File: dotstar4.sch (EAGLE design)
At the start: 13 parts, among them J1 IN/OUT, J2 OUT

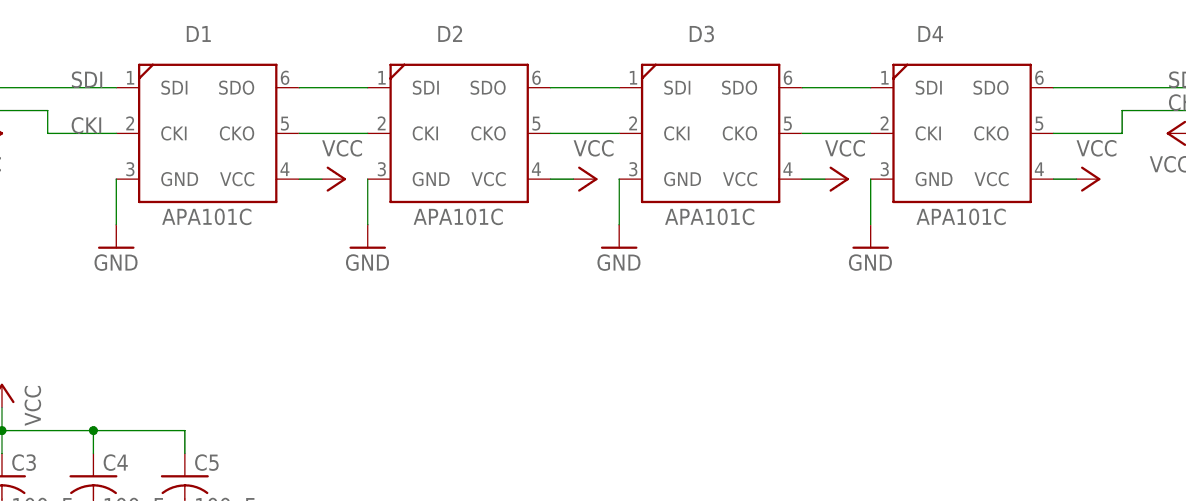
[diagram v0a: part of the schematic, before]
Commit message: Replace erroneously named APA101C device with APA102C.
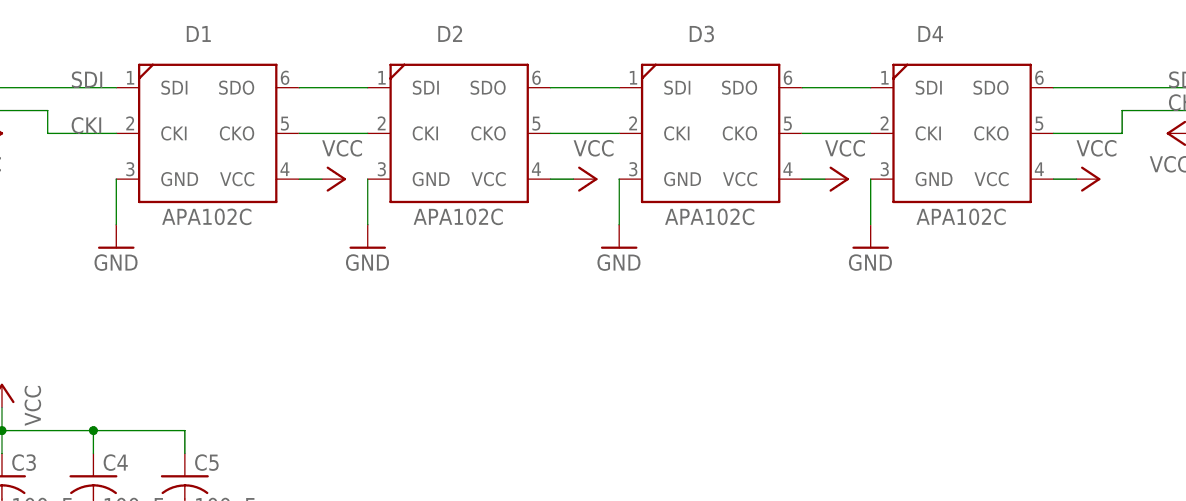
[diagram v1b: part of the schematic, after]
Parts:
- D1, D2, D3, D4: value APA101C -> APA102C; device _jc:APA101C -> _jc:APA102C
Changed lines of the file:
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@@
 <parts>
 <part name="FRAME1" library="frames" library_urn="urn:adsk.eagle:library:229" deviceset="FRAME_A_L" device="" value="MyFrame"/>
-<part name="D1" library="_jc" deviceset="APA101C" device=""/>
-<part name="D2" library="_jc" deviceset="APA101C" device=""/>
-<part name="D3" library="_jc" deviceset="APA101C" device=""/>
-<part name="D4" library="_jc" deviceset="APA101C" device=""/>
+<part name="D1" library="_jc" deviceset="APA102C" device=""/>
+<part name="D2" library="_jc" deviceset="APA102C" device=""/>
+<part name="D3" library="_jc" deviceset="APA102C" device=""/>
+<part name="D4" library="_jc" deviceset="APA102C" device=""/>
 <part name="P+1" library="supply1" library_urn="urn:adsk.eagle:library:371" deviceset="VCC" device=""/>
 <part name="GND1" library="supply1" library_urn="urn:adsk.eagle:library:371" deviceset="GND" device=""/>
